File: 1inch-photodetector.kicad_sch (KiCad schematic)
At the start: 21 parts, among them J1 Conn_01x03, J2 Conn_Coaxial, U1 ADA4898-2, U2 LT3032-12

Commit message: Removed GND-Earth connection
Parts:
- added H1: MountingHole_Pad, Connector_Wire:SolderWirePad_1x01_SMD_1x2mm, symbol Mechanical:MountingHole_Pad
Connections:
- new net Earth: H1.1
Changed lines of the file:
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@@
+	(wire
+		(pts
+			(xy 201.93 100.33) (xy 201.93 104.14)
+		)
+		(stroke
+			(width 0)
+			(type default)
+		)
+	)
 	(wire
 		(pts
@@
 	)
 	(symbol
+		(lib_id "Mechanical:MountingHole_Pad")
+		(at 201.93 97.79 0)
+		(unit 1)
+		(exclude_from_sim no)
+		(in_bom no)
+		(on_board yes)
+		(dnp no)
+		(fields_autoplaced yes)
+		(property "Reference" "H1"
+			(at 204.47 95.2499 0)
+			(effects
+				(font
+					(size 1.27 1.27)
+				)
+				(justify left)
+			)
+		)
+		(property "Value" "MountingHole_Pad"
+			(at 204.47 97.7899 0)
+			(effects
+				(font
+					(size 1.27 1.27)
+				)
+				(justify left)
+			)
+		)
+		(property "Footprint" "Connector_Wire:SolderWirePad_1x01_SMD_1x2mm"
+			(at 201.93 97.79 0)
+			(effects
+				(font
+					(size 1.27 1.27)
+				)
+				(hide yes)
+			)
+		)
+		(property "Datasheet" "~"
+			(at 201.93 97.79 0)
+			(effects
+				(font
+					(size 1.27 1.27)
+				)
+				(hide yes)
+			)
+		)
+		(property "Description" "Mounting Hole with connection"
+			(at 201.93 97.79 0)
+			(effects
+				(font
+					(size 1.27 1.27)
+				)
+				(hide yes)
+			)
+		)
+		(property "MFN" ""
+			(at 201.93 97.79 0)
+			(effects
+				(font
+					(size 1.27 1.27)
+				)
+				(hide yes)
+			)
+		)
+		(property "PN" ""
+			(at 201.93 97.79 0)
+			(effects
+				(font
+					(size 1.27 1.27)
+				)
+				(hide yes)
+			)
+		)
+		(property "RoHS" ""
+			(at 201.93 97.79 0)
+			(effects
+				(font
+					(size 1.27 1.27)
+				)
+				(hide yes)
+			)
+		)
+		(property "Temperature" ""
+			(at 201.93 97.79 0)
+			(effects
+				(font
+					(size 1.27 1.27)
+				)
+				(hide yes)
+			)
+		)
+		(pin "1"
+		)
+		(instances
+			(project ""
+				(path "/bc1f768a-38ac-49f6-bd7e-5ad2d645b686"
+					(reference "H1")
+					(unit 1)
+				)
+			)
+		)
+	)
+	(symbol
 		(lib_id "Device:C")
 		(at 111.76 153.67 0)
@@
 					(unit 1)
 				)
+			)
+		)
+	)
+	(symbol
+		(lib_id "power:Earth")
+		(at 201.93 104.14 0)
+		(unit 1)
+		(exclude_from_sim no)
+		(in_bom yes)
+		(on_board yes)
+		(dnp no)
+		(fields_autoplaced yes)
+		(property "Reference" "#PWR010"
+			(at 201.93 110.49 0)
+			(effects
+				(font
+					(size 1.27 1.27)
+				)
+				(hide yes)
+			)
+		)
+		(property "Value" "Earth"
+			(at 201.93 109.22 0)
+			(effects
+				(font
+					(size 1.27 1.27)
+				)
+			)
+		)
+		(property "Footprint" ""
+			(at 201.93 104.14 0)
+			(effects
+				(font
+					(size 1.27 1.27)
+				)
+				(hide yes)
+			)
+		)
+		(property "Datasheet" "~"
+			(at 201.93 104.14 0)
+			(effects
+				(font
+					(size 1.27 1.27)
+				)
+				(hide yes)
+			)
+		)
+		(property "Description" "Power symbol creates a global label with name \"Earth\""
+			(at 201.93 104.14 0)
+			(effects
+				(font
+					(size 1.27 1.27)
+				)
+				(hide yes)
+			)
+		)
+		(pin "1"
+		)
+		(instances
+			(project ""
+				(path "/bc1f768a-38ac-49f6-bd7e-5ad2d645b686"
+					(reference "#PWR010")
+					(unit 1)
+				)

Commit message: Added PWR flag
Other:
- moved on the sheet: H1
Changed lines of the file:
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@@
+	)
+	(junction
+		(at 201.93 101.6)
+		(diameter 0)
+		(color 0 0 0 0)
 	)
 	(junction
@@
 	(wire
 		(pts
-			(xy 201.93 100.33) (xy 201.93 104.14)
+			(xy 208.28 100.33) (xy 208.28 101.6)
 		)
 		(stroke
@@
 	(wire
 		(pts
+			(xy 208.28 101.6) (xy 201.93 101.6)
+		)
+		(stroke
+			(width 0)
+			(type default)
+		)
+	)
+	(wire
+		(pts
 			(xy 91.44 82.55) (xy 100.33 82.55)
 		)
@@
 	(wire
 		(pts
+			(xy 201.93 101.6) (xy 201.93 104.14)
+		)
+		(stroke
+			(width 0)
+			(type default)
+		)
+	)
+	(wire
+		(pts
 			(xy 60.96 73.66) (xy 60.96 77.47)
 		)
@@
 		(pts
 			(xy 73.66 43.18) (xy 73.66 54.61)
+		)
+		(stroke
+			(width 0)
+			(type default)
+		)
+	)
+	(wire
+		(pts
+			(xy 201.93 97.79) (xy 201.93 101.6)
 		)
 		(stroke
@@
 	(symbol
 		(lib_id "Mechanical:MountingHole_Pad")
-		(at 201.93 97.79 0)
+		(at 208.28 97.79 0)
 		(unit 1)
 		(exclude_from_sim no)
@@
 		(fields_autoplaced yes)
 		(property "Reference" "H1"
-			(at 204.47 95.2499 0)
+			(at 210.82 95.2499 0)
 			(effects
 				(font
@@
 		)
 		(property "Value" "MountingHole_Pad"
-			(at 204.47 97.7899 0)
+			(at 210.82 97.7899 0)
 			(effects
 				(font
@@
 		)
 		(property "Footprint" "Connector_Wire:SolderWirePad_1x01_SMD_1x2mm"
-			(at 201.93 97.79 0)
+			(at 208.28 97.79 0)
 			(effects
 				(font
@@
 		)
 		(property "Datasheet" "~"
-			(at 201.93 97.79 0)
+			(at 208.28 97.79 0)
 			(effects
 				(font
@@
 		)
 		(property "Description" "Mounting Hole with connection"
-			(at 201.93 97.79 0)
+			(at 208.28 97.79 0)
 			(effects
 				(font
@@
 		)
 		(property "MFN" ""
-			(at 201.93 97.79 0)
+			(at 208.28 97.79 0)
 			(effects
 				(font
@@
 		)
 		(property "PN" ""
-			(at 201.93 97.79 0)
+			(at 208.28 97.79 0)
 			(effects
 				(font
@@
 		)
 		(property "RoHS" ""
-			(at 201.93 97.79 0)
+			(at 208.28 97.79 0)
 			(effects
 				(font
@@
 		)
 		(property "Temperature" ""
-			(at 201.93 97.79 0)
+			(at 208.28 97.79 0)
 			(effects
 				(font
@@
 					(unit 1)
 				)
+			)
+		)
+	)
+	(symbol
+		(lib_id "power:PWR_FLAG")
+		(at 201.93 97.79 0)
+		(unit 1)
+		(exclude_from_sim no)
+		(in_bom yes)
+		(on_board yes)
+		(dnp no)
+		(fields_autoplaced yes)
+		(property "Reference" "#FLG04"
+			(at 201.93 95.885 0)
+			(effects
+				(font
+					(size 1.27 1.27)
+				)
+				(hide yes)
+			)
+		)
+		(property "Value" "PWR_FLAG"
+			(at 201.93 92.71 0)
+			(effects
+				(font
+					(size 1.27 1.27)
+				)
+			)
+		)
+		(property "Footprint" ""
+			(at 201.93 97.79 0)
+			(effects
+				(font
+					(size 1.27 1.27)
+				)
+				(hide yes)
+			)
+		)
+		(property "Datasheet" "~"
+			(at 201.93 97.79 0)
+			(effects
+				(font
+					(size 1.27 1.27)
+				)
+				(hide yes)
+			)
+		)
+		(property "Description" "Special symbol for telling ERC where power comes from"
+			(at 201.93 97.79 0)
+			(effects
+				(font
+					(size 1.27 1.27)
+				)
+				(hide yes)
+			)
+		)
+		(pin "1"
+		)
+		(instances
+			(project ""
+				(path "/bc1f768a-38ac-49f6-bd7e-5ad2d645b686"
+					(reference "#FLG04")
+					(unit 1)
+				)

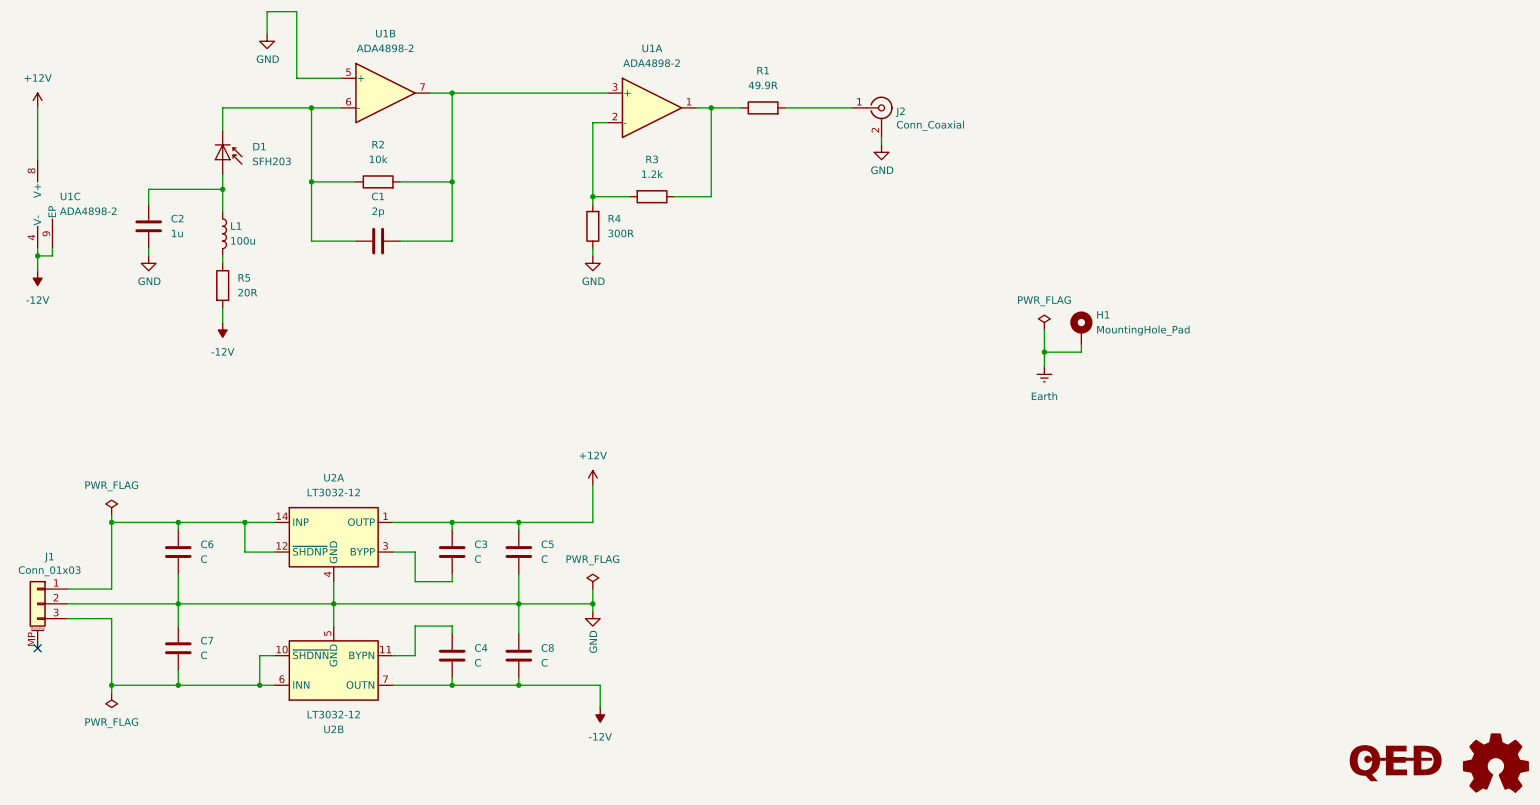
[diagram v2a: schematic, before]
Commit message: Increased size to 25.4 mm
- Added optional jumpers to connect GND to Earth
- Added more ground stitching vias
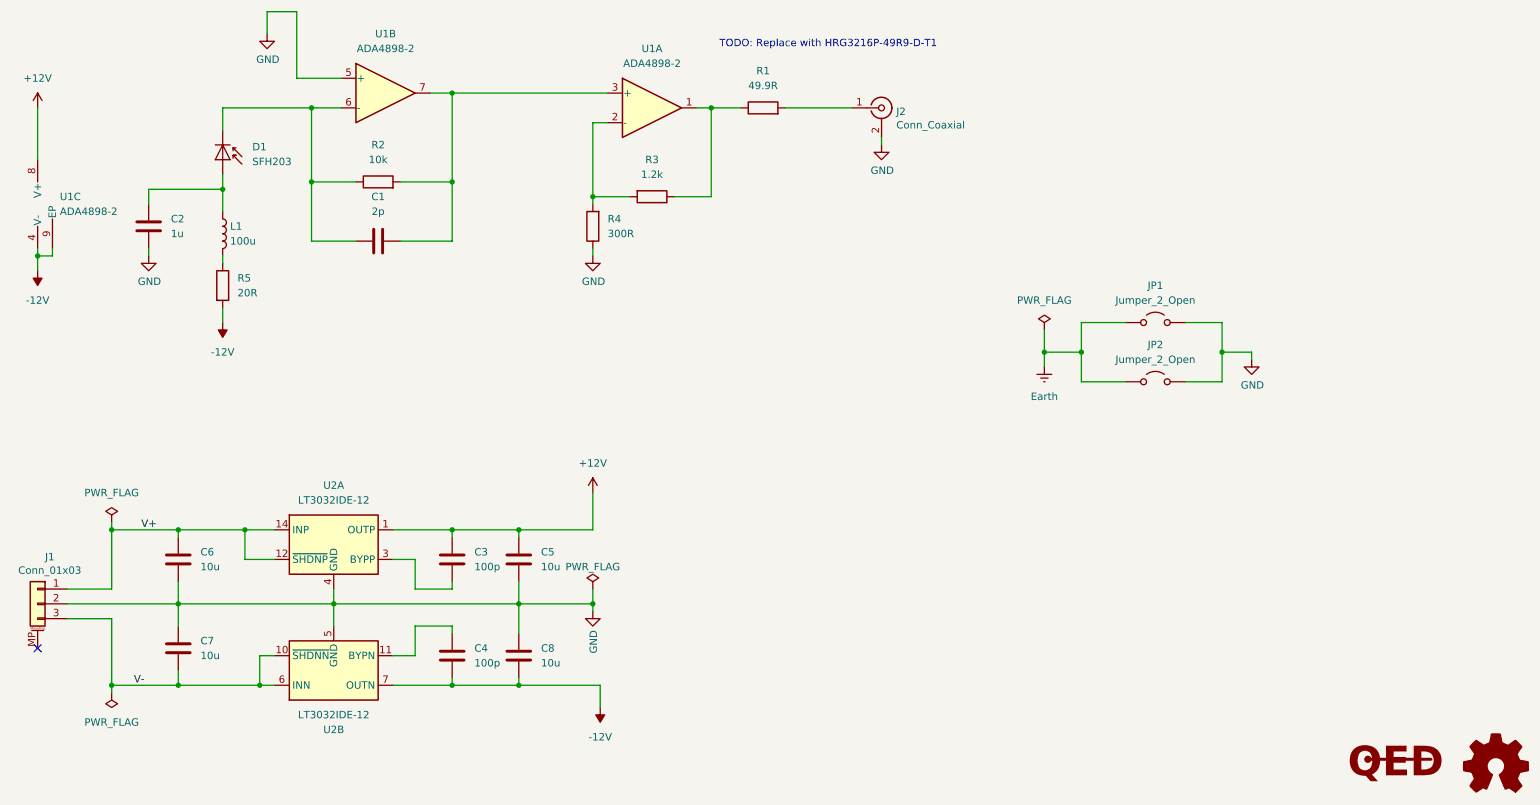
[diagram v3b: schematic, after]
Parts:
- removed H1: MountingHole_Pad, Connector_Wire:SolderWirePad_1x01_SMD_1x2mm, symbol Mechanical:MountingHole_Pad
- added JP1, JP2: Jumper_2_Open, Resistor_SMD:R_0402_1005Metric, symbol Jumper:Jumper_2_Open
- C1: MFN (none) -> Yageo; PN (none) -> AC0603BRNPO9BN2R0; RoHS (none) -> Yes; Temperature (none) -> Top = –55 °C to 125 °C
- C2, L1: Temperature -55,125 -> Top = –55 °C to 125 °C
- C3, C4: value C -> 100p; MFN (none) -> Murata Electronics; PN (none) -> GCM1885C2A101JA16D; RoHS (none) -> Yes; Temperature (none) -> Top = –55 °C to 125 °C
- C5, C6, C7, C8: value C -> 10u; MFN (none) -> TDK; PN (none) -> CGA4J1X7S1E106K125AC; RoHS (none) -> Yes; Temperature (none) -> Top = –55 °C to 125 °C
- D1: MFN (none) -> ams Osram; PN (none) -> SFH 203 FA; RoHS (none) -> Yes; Temperature (none) -> Top = –40 °C to 100 °C; Tstorage = –40 °C to 100 °C
- J1: MFN (none) -> Molex; PN (none) -> 53398-0371; RoHS (none) -> Yes; Temperature (none) -> Top = –40 °C to 105 °C; Tstorage = –5 °C to 35 °C
- J2: MFN (none) -> TE Connectivity; PN (none) -> CONSMP001-SMD-G-T; RoHS (none) -> Yes; Temperature (none) -> Tstorage = –65 °C to 155 °C
- R1: footprint Resistor_SMD:R_0603_1608Metric -> Resistor_SMD:R_1206_3216Metric; MFN (none) -> Yageo; PN (none) -> HRG3216P-49R9-D-T1; RoHS (none) -> Yes; Temperature (none) -> Top = –55 °C to 155 °C
- R2: MFN (none) -> Susumu; PN (none) -> RG1608P-103-D-T5; RoHS (none) -> Yes; Temperature (none) -> Top = –55 °C to 155 °C
- R3: MFN (none) -> Susumu; PN (none) -> RG1608P-122-D-T5; RoHS (none) -> Yes; Temperature (none) -> Top = –55 °C to 155 °C
- R4: MFN (none) -> Susumu; PN (none) -> RG1608P-301-B-T5; RoHS (none) -> Yes; Temperature (none) -> Top = –55 °C to 155 °C
- R5: MFN (none) -> Susumu; PN (none) -> RG1608Q-200-D-T5; RoHS (none) -> Yes; Temperature (none) -> Top = –55 °C to 155 °C
- U1: Alternative (none) -> Analog Devices ADA4898-2YRDZ-R7; MFN (none) -> Analog Devices; PN (none) -> ADA4898-2YRDZ; RoHS (none) -> Yes; Temperature (none) -> Top = –40 °C to 105 °C; Tstorage = –65 °C to 150 °C
- U2: value LT3032-12 -> LT3032IDE-12; Alternative (none) -> Analog Devices LT3032EDE-12#PBF; MFN (none) -> Analog Devices; PN (none) -> LT3032IDE-12#PBF; RoHS (none) -> Yes; Temperature (none) -> Top = –40 °C to 125 °C
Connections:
- net Earth: now also JP1.1 (A), JP2.1 (A)
- net GND: now also JP1.2 (B), JP2.2 (B)
- net V+: now reaches C6.1, J1.1 (Pin_1), U2.12 (~{SHDNP}), U2.14 (INP)
- net V-: now reaches C7.2, J1.3 (Pin_3), U2.10 (~{SHDNN}), U2.6 (INN), U2.9 (INN)
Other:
- note added: "TODO: Replace with HRG3216P-49R9-D-T1"
- moved on the sheet: C3, C5, C6, U2A
